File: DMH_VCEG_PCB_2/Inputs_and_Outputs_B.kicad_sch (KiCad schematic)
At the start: 38 parts, among them J11 TS_Jack_6.35mm_Sw, J12 TS_Jack_6.35mm_Sw, J13 TS_Jack_6.35mm_Sw, J14 TS_Jack_6.35mm_Sw, J15 TS_Jack_6.35mm_Sw, J16 TS_Jack_6.35mm_Sw, J17 TS_Jack_6.35mm_Sw, J18 TS_Jack_6.35mm_Sw, J19 TS_Jack_6.35mm_Sw, J20 TS_Jack_6.35mm_Sw, J24 Conn_01x10_PinHeader, J25 Conn_01x10_PinHeader, J26 Conn_01x10_PinHeader, J27 Conn_01x06_PinHeader, U18 TL074, U21 TL074

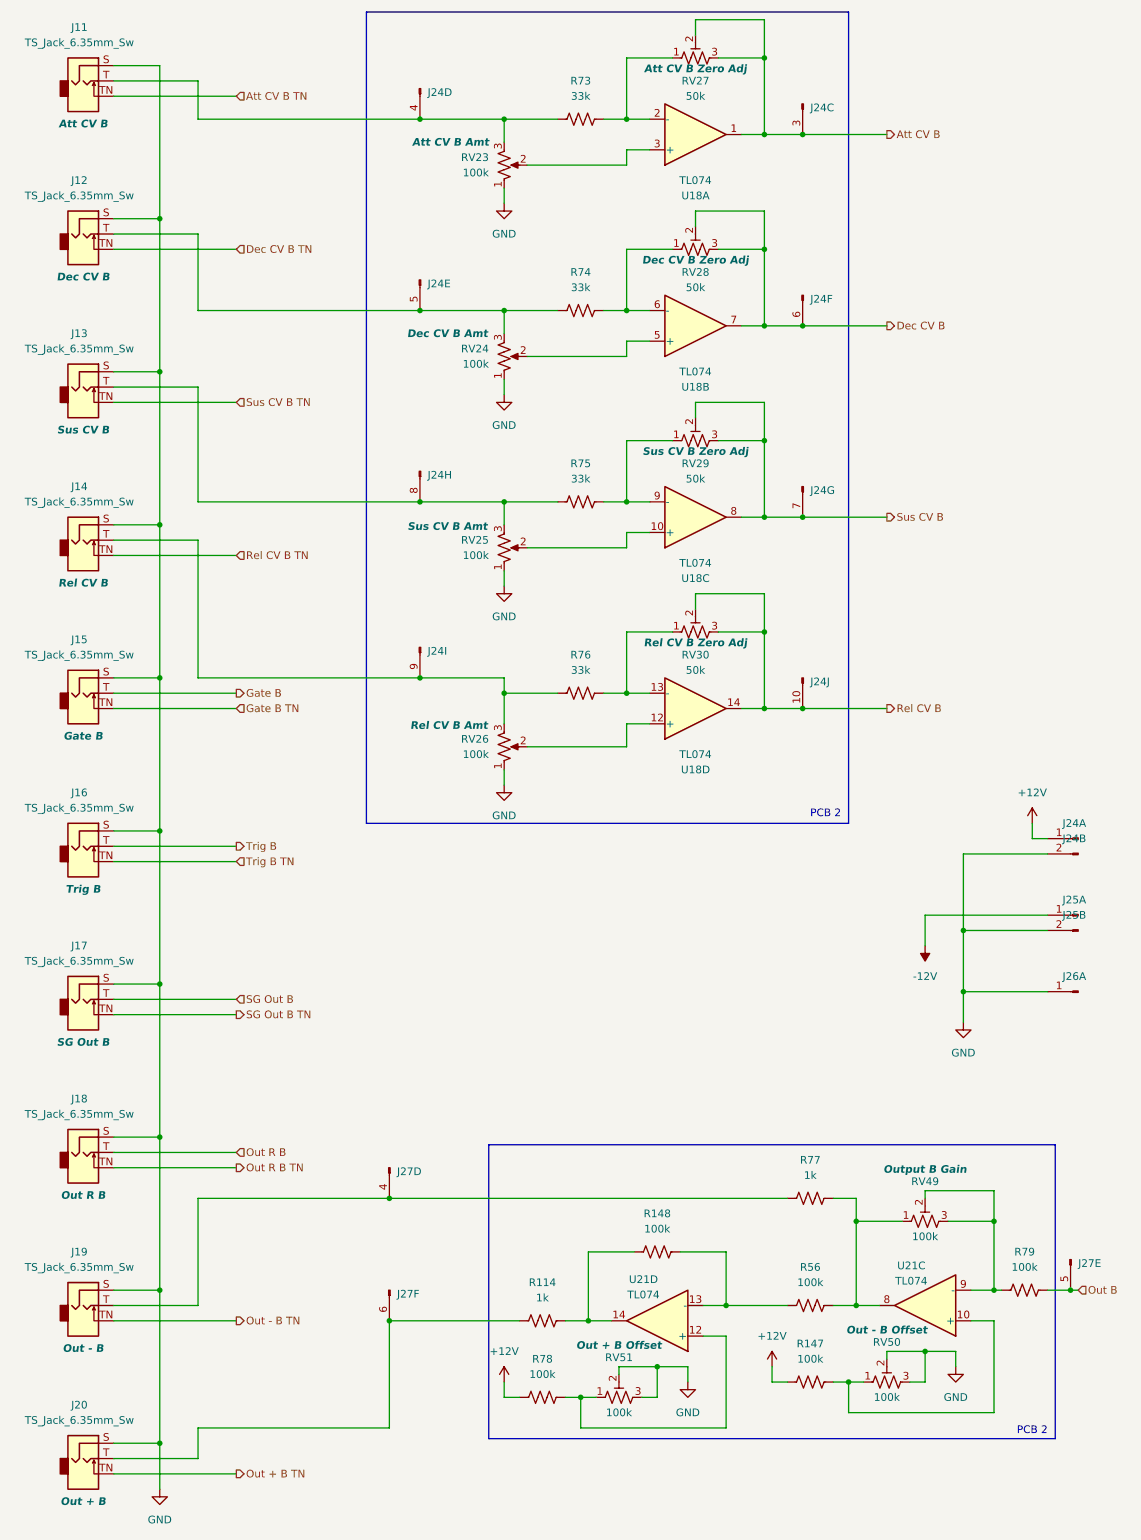
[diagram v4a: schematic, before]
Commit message: Synced PCB 2 project with PCB 1
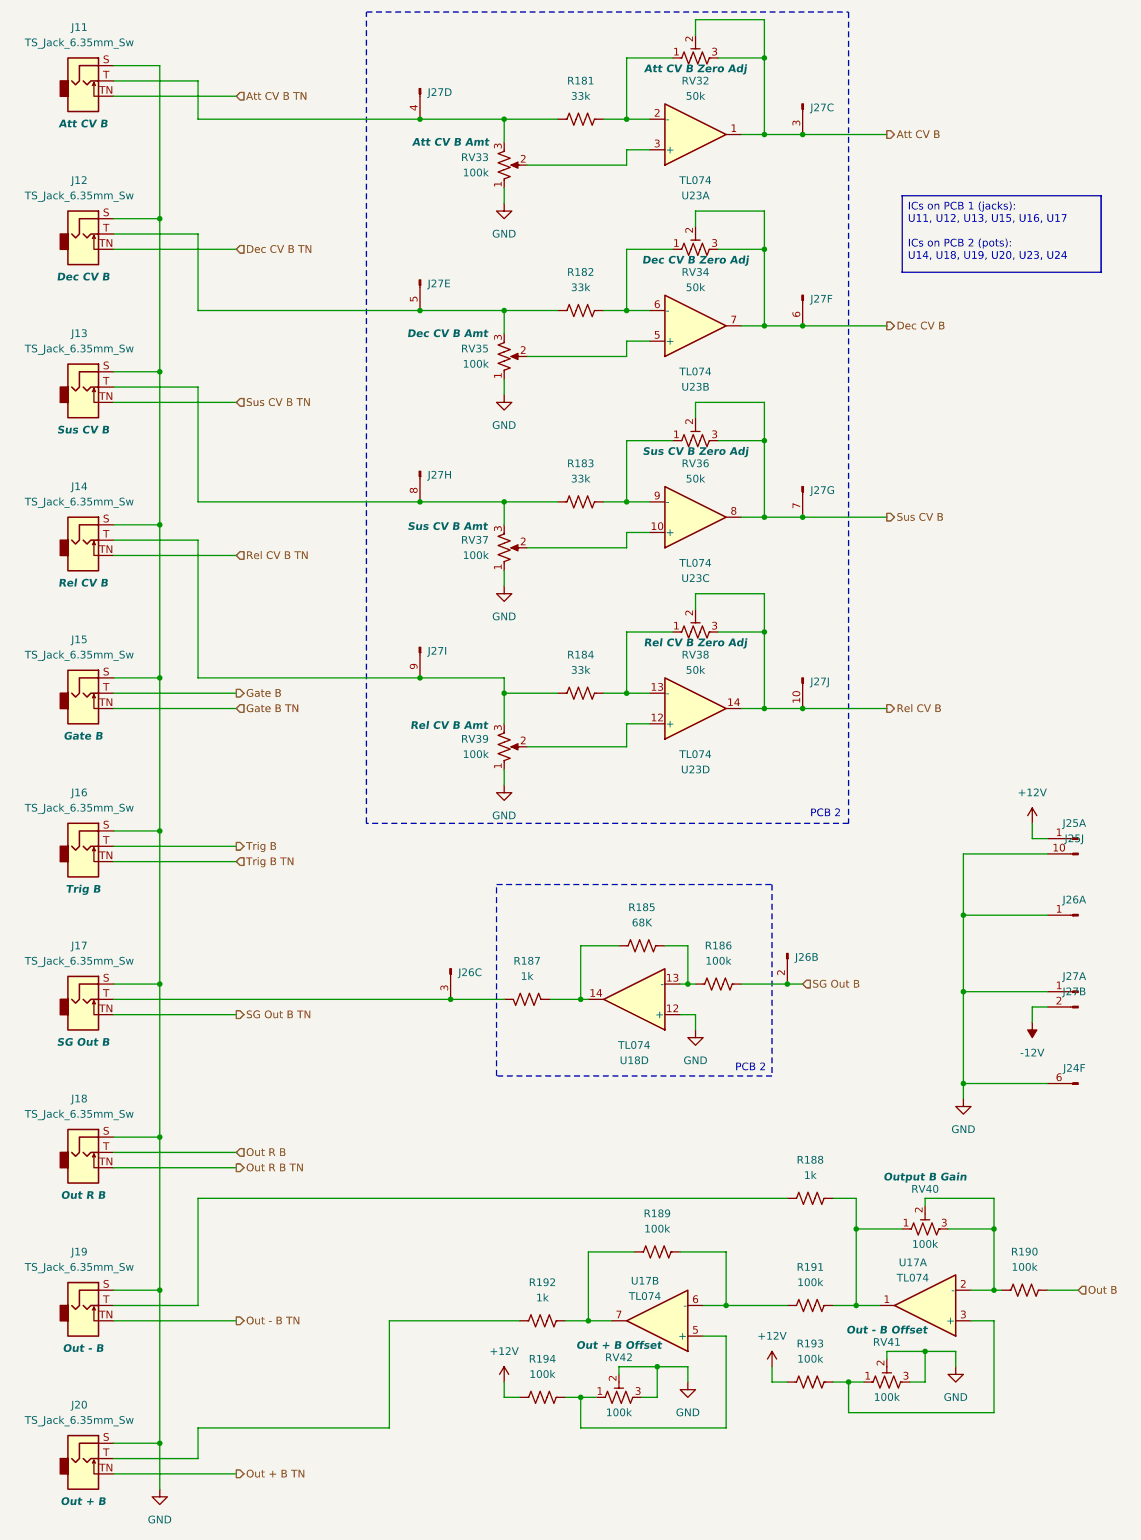
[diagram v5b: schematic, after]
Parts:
- removed unit 1 of J24
- removed unit 2 of J24
- removed unit 2 of J25
- removed J27: Conn_01x06_PinHeader, Connector_PinSocket_2.54mm:PinSocket_1x06_P2.54mm_Vertical, symbol SynthStuff:Conn_01x06_PinHeader
- removed R148, R56: 100k, Resistor_THT:R_Axial_DIN0207_L6.3mm_D2.5mm_P7.62mm_Horizontal, symbol Device:R_US
- removed U21: TL074, symbol Amplifier_Operational:TL074
- added J24: Conn_01x06_PinHeader, Connector_PinHeader_2.54mm:PinHeader_1x06_P2.54mm_Vertical, symbol SynthStuff:Conn_01x06_PinHeader
- added unit 10 of J25
- added unit 3 of J26
- added unit 2 of J26
- added unit 2 of J27
- added unit 1 of J27
- added R185: 68K, Resistor_THT:R_Axial_DIN0207_L6.3mm_D2.5mm_P7.62mm_Horizontal, symbol Device:R_US
- added R186, R189, R191: 100k, Resistor_THT:R_Axial_DIN0207_L6.3mm_D2.5mm_P7.62mm_Horizontal, symbol Device:R_US
- added R187: 1k, Resistor_THT:R_Axial_DIN0207_L6.3mm_D2.5mm_P7.62mm_Horizontal, symbol Device:R_US
- added U17, U18: TL074, Package_DIP:DIP-14_W7.62mm_Socket, symbol Amplifier_Operational:TL074
- J25: footprint Connector_PinSocket_2.54mm:PinSocket_1x10_P2.54mm_Vertical -> Connector_PinHeader_2.54mm:PinHeader_1x10_P2.54mm_Vertical
- RV40: renamed from RV49; footprint Potentiometer_THT:Potentiometer_Bourns_3296X_Horizontal -> Potentiometer_THT:Potentiometer_Bourns_3296W_Vertical
- RV41: renamed from RV50; footprint Potentiometer_THT:Potentiometer_Bourns_3296X_Horizontal -> Potentiometer_THT:Potentiometer_Bourns_3296W_Vertical
- RV42: renamed from RV51; footprint Potentiometer_THT:Potentiometer_Bourns_3296X_Horizontal -> Potentiometer_THT:Potentiometer_Bourns_3296W_Vertical
- renumbered J24 to J27, R73 to R181, R74 to R182, R75 to R183, R76 to R184, R77 to R188, R79 to R190, R114 to R192, R147 to R193, R78 to R194, RV27 to RV32, RV23 to RV33, RV28 to RV34, RV24 to RV35, RV29 to RV36, RV25 to RV37, RV30 to RV38, RV26 to RV39, U18 to U23
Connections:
- net +12V: now also J25.1 (Pin_1)
- net -12V: now also J27.2 (Pin_2); no longer J25.1 (Pin_1)
- net GND: now also J24.6 (Pin_6), J25.10 (Pin_10), J27.1 (Pin_1), U18.12 (+)
- net SG Out B: now also J26.2 (Pin_2), R186.1; no longer J17.T
- net at R194.1, RV42.1: now also U17.5 (+)
- net at R192.1: now also R189.2, U17.7
- net at R193.1, RV41.1: now also U17.3 (+)
- net at R188.1, RV40.1: now also R191.1, U17.1
- net at R190.2, RV40.2, RV40.3: now also U17.2 (-)
- new net: R185.1, R186.2, U18.13 (-)
- new net: R185.2, R187.2, U18.14
- new net: J17.T, J26.3 (Pin_3), R187.1
- new net: R189.1, R191.2, U17.6 (-)
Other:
- moved on the sheet: RV40

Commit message: Started placement on PCB 2
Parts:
- J24: footprint Connector_PinHeader_2.54mm:PinHeader_1x06_P2.54mm_Vertical -> Connector_PinSocket_2.54mm:PinSocket_1x06_P2.54mm_Vertical
- J25: footprint Connector_PinHeader_2.54mm:PinHeader_1x10_P2.54mm_Vertical -> Connector_PinSocket_2.54mm:PinSocket_1x10_P2.54mm_Vertical
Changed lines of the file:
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@@
 			)
 		)
-		(property "Footprint" "Connector_PinHeader_2.54mm:PinHeader_1x06_P2.54mm_Vertical"
+		(property "Footprint" "Connector_PinSocket_2.54mm:PinSocket_1x06_P2.54mm_Vertical"
 			(at 190.5 191.77 0)
 			(effects
@@
 			)
 		)
-		(property "Footprint" "Connector_PinHeader_2.54mm:PinHeader_1x10_P2.54mm_Vertical"
+		(property "Footprint" "Connector_PinSocket_2.54mm:PinSocket_1x10_P2.54mm_Vertical"
 			(at 190.5 151.13 0)
 			(effects
@@
 			)
 		)
-		(property "Footprint" "Connector_PinHeader_2.54mm:PinHeader_1x10_P2.54mm_Vertical"
+		(property "Footprint" "Connector_PinSocket_2.54mm:PinSocket_1x10_P2.54mm_Vertical"
 			(at 190.5 153.67 0)
 			(effects

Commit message: PCB 2 placement in progress
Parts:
- RV32: Function Att CV B Zero Adj -> Att CV B Zero
- RV34: Function Dec CV B Zero Adj -> Dec CV B Zero
- RV36: Function Sus CV B Zero Adj -> Sus CV B Zero
- RV38: Function Rel CV B Zero Adj -> Rel CV B Zero
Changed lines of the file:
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@@
 			)
 		)
-		(property "Function" "Sus CV B Zero Adj"
+		(property "Function" "Sus CV B Zero"
 			(at 127 86.868 90)
 			(effects
@@
 			)
 		)
-		(property "Function" "Dec CV B Zero Adj"
+		(property "Function" "Dec CV B Zero"
 			(at 127 55.118 90)
 			(effects
@@
 			)
 		)
-		(property "Function" "Rel CV B Zero Adj"
+		(property "Function" "Rel CV B Zero"
 			(at 127 118.618 90)
 			(effects
@@
 			)
 		)
-		(property "Function" "Att CV B Zero Adj"
+		(property "Function" "Att CV B Zero"
 			(at 127 23.368 90)
 			(effects

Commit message: Synced changes to PCB 2
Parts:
- added R11: 100k, Resistor_THT:R_Axial_DIN0207_L6.3mm_D2.5mm_P7.62mm_Horizontal, symbol Device:R_US
- added R18: 68k, Resistor_THT:R_Axial_DIN0207_L6.3mm_D2.5mm_P7.62mm_Horizontal, symbol Device:R_US
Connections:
- net +12V: now also R18.1
- net GND: now also R11.2; no longer U18.12 (+)
- new net: R11.1, R18.2, U18.12 (+)
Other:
- moved on the sheet: U18D
